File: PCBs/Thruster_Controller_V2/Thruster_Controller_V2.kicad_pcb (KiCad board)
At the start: 4 copper layers, 35.5 x 37 mm, 106 parts, among them J1 PHASE_A, J2 PHASE_B, J3 PHASE_C, J4 Conn_01x01, J5 Pogo Conn, J6 Conn_01x01, J7 Conn_01x01, J8 Conn_01x01, Q1 SIZF906DT, Q2 SIZF906DT, Q3 SIZF906DT, U1 NCP718AMT330, U2 TMS320F280041C, U3 DRV8320S, U8 MCP2562, Y1 20 MHz

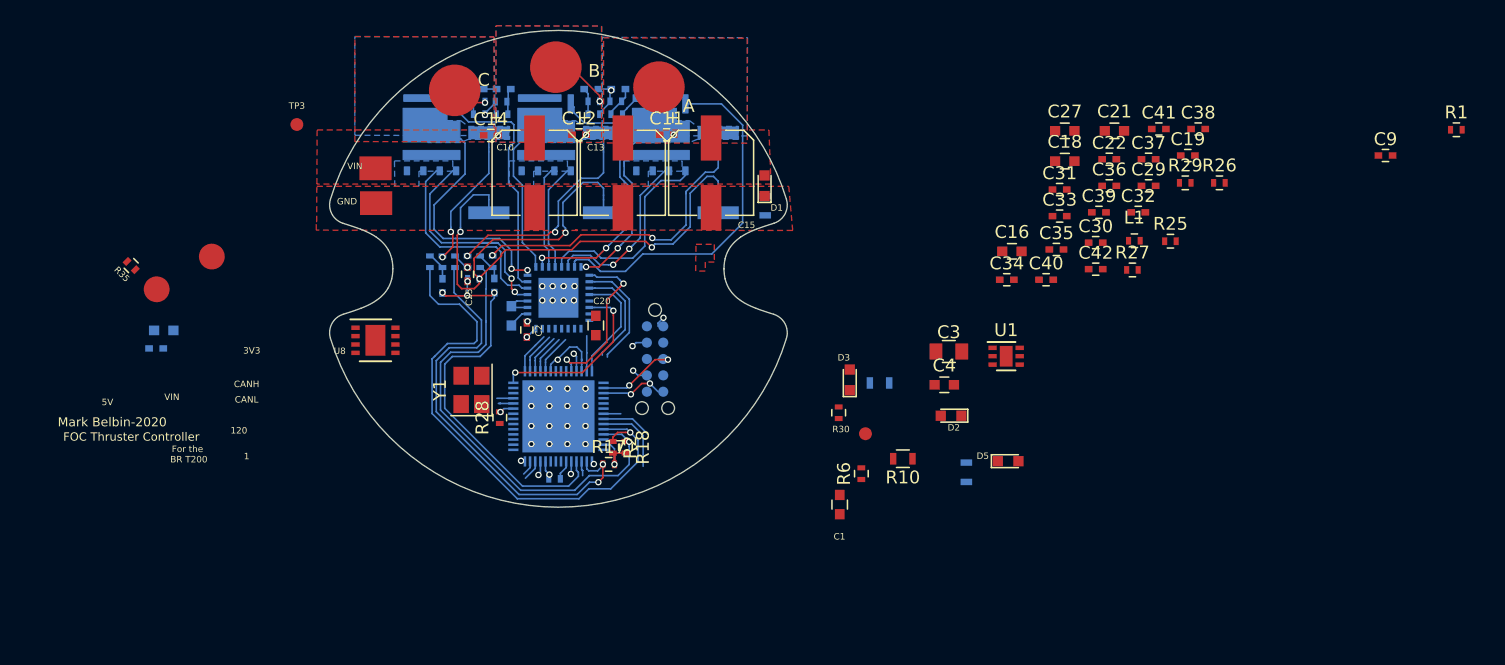
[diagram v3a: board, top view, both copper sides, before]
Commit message: Layout Complete
- Initial layout complete
- Most routing complete, still need to clean up everything.
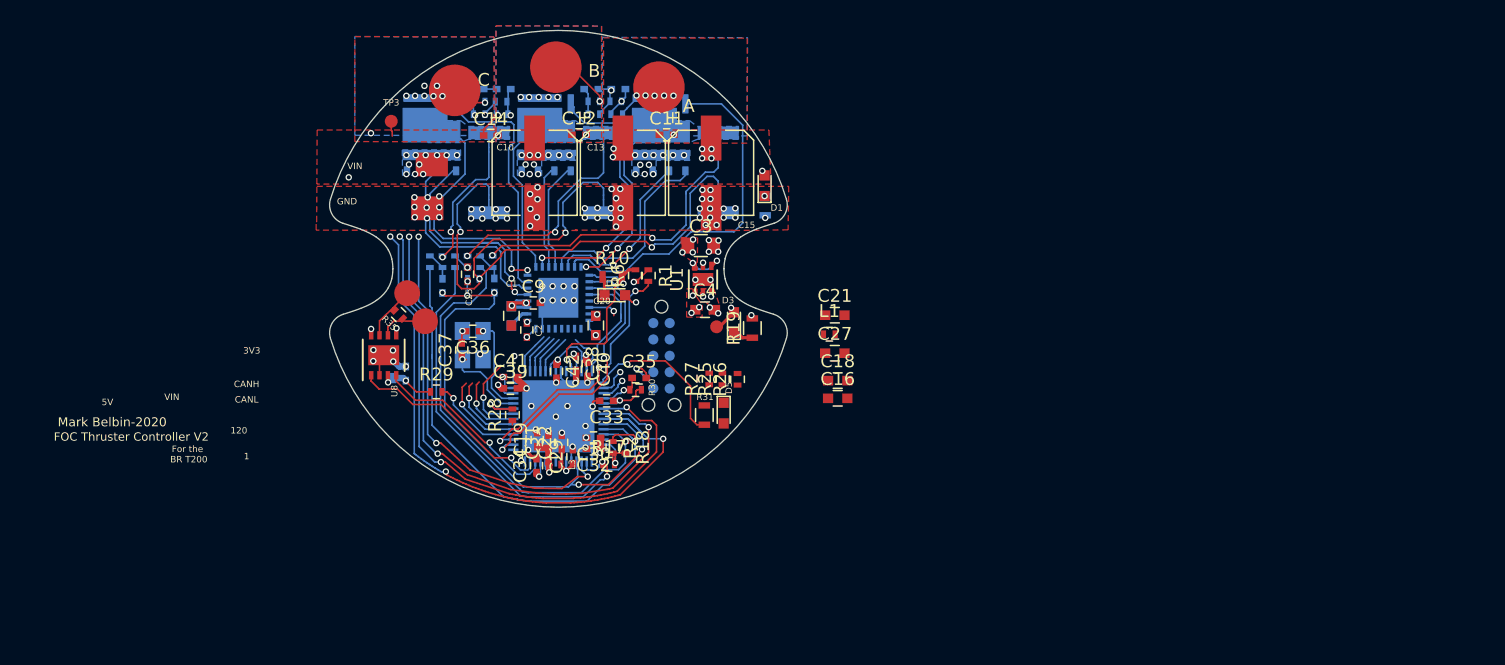
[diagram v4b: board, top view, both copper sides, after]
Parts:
- L3, R19, R31: moved to F.Cu
- Y1: footprint Crystals:Crystal_SMD_SeikoEpson_FA238-4pin_3.2x2.5mm -> Thruster_Controller:Crystal_SMD_SeikoEpson_FA238-4pin_3.2x2.5mm; moved to B.Cu
- moved C9 67.1 mm to (98.0, 100.9)
- moved R1 63.7 mm to (107.0, 98.8), turned to 270 degrees
- moved R29 60.3 mm to (90.5, 107.8)
- moved C37 55.3 mm to (92.5, 104.5), turned to 90 degrees
- moved C19 55.1 mm to (98.3, 111.5), turned to 90 degrees
- moved C41 53.9 mm to (96.3, 106.7)
- moved C38 51.6 mm to (101.4, 105.6), turned to 270 degrees
- moved C36 50.7 mm to (93.3, 103.1), turned to 180 degrees
- moved C29 49.4 mm to (101.1, 112.8), turned to 90 degrees
- moved C22 47.8 mm to (100.2, 111.7), turned to 90 degrees
- moved C39 47.7 mm to (96.3, 107.5)
- moved C32 46.1 mm to (102.7, 112.2), turned to 180 degrees
- moved C31 44.3 mm to (99.2, 111.7), turned to 90 degrees
- moved C42 42.6 mm to (99.8, 106.2), turned to 270 degrees
- moved C30 41.8 mm to (102.7, 111.4), turned to 180 degrees
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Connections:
- C17 pad 1: /Powertrain/VSEN_C -> /Powertrain/VSEN_PVDD
- R15 pad 2: /Powertrain/VSEN_C -> /Powertrain/VSEN_PVDD
- R16 pad 1: /Powertrain/VSEN_C -> /Powertrain/VSEN_PVDD
- U2 pad 6: /Powertrain/VSEN_C -> /Powertrain/VSEN_PVDD
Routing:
- net /Powertrain/VSEN_PVDD: track 0.00 -> 67.2 mm, vias 0 -> 4
- net /Powertrain/VSEN_B: track 3.41 -> 70.6 mm, vias 0 -> 4
- net /Powertrain/VSEN_A: track 6.06 -> 69.1 mm, vias 0 -> 4
- net /Powertrain/VSEN_C: track 5.67 -> 63.5 mm, vias 0 -> 4
- net GND: track 11.7 -> 29.5 mm, vias 30 -> 98
- net +3V3: track 2.94 -> 20.7 mm, vias 2 -> 13
- net /Powertrain/SPI_MOSI: track 8.13 -> 24.9 mm, vias 0 -> 2
- net /Powertrain/SPI_MISO: track 8.86 -> 24.3 mm, vias 0 -> 3
- net /TXCAN: track 1.18 -> 16.3 mm, vias 0 -> 1
- net /RXCAN: track 1.61 -> 15.1 mm, vias 0 -> 1
- net /TI_MCU/GPIO6: track 0.00 -> 12.2 mm, vias 0 -> 1
- net +BATT: track 2.71 -> 12.3 mm, vias 0 -> 50
- net /Powertrain/EN_GATE: track 13.8 -> 4.47 mm
- net /TI_MCU/GPIO24: track 0.00 -> 7.20 mm, vias 0 -> 1
- net /TCK: track 0.00 -> 6.63 mm, vias 0 -> 1
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- added copper zone on In1.Cu, net +3.3VA
- added copper zone on F.Cu, net +3V3
- added copper zone on In1.Cu, net +3V3
- removed copper zone on In2.Cu, net +3V3
- removed copper zone on In2.Cu, net +BATT
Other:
- board text added: "FOC Thruster Controller V2"
- board text removed: "FOC Thruster Controller"

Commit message: Initial Routing and Layout
- Completed all routing, all connections made and zero DRC errors.
- Some courtyard errors but they are irrelevant
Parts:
- C5: moved to F.Cu
- L1: moved to B.Cu
- moved C21 35.3 mm to (87.0, 109.1), turned to 270 degrees
- moved C27 33.6 mm to (88.3, 110.4), turned to 270 degrees
- moved L1 33.5 mm to (88.0, 108.5), turned to 270 degrees
- moved C18 10.5 mm to (111.7, 110.1)
- moved R25 9.00 mm to (108.7, 98.8), turned to 270 degrees
- moved C16 7.73 mm to (114.3, 106.0), turned to 270 degrees
- moved R26 6.10 mm to (109.3, 110.8)
- moved R28 4.36 mm to (92.1, 109.7), turned to 0 degrees
- moved R31 2.25 mm to (111.4, 107.3)
- moved R27 2.15 mm to (111.0, 104.8)
- moved R7 1.94 mm to (115.1, 91.7)
- moved D5 1.88 mm to (112.8, 107.6)
- moved C20 1.72 mm to (101.5, 101.7), turned to 180 degrees
- moved C5 1.40 mm to (95.0, 101.9)
- moved R30 0.46 mm to (106.5, 107.6)
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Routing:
- net /TDO: track 5.95 -> 34.4 mm, vias 1 -> 2
- net /TCK: track 6.63 -> 32.1 mm, vias 1 -> 2
- net /Powertrain/SPI_CS: track 0.32 -> 21.9 mm, vias 1 -> 4
- net /TMS: track 5.34 -> 25.8 mm, vias 1 -> 3
- net /TDI: track 6.39 -> 26.5 mm, vias 1 -> 3
- net +3V3: track 20.7 -> 31.7 mm, vias 13 -> 21
- net /Powertrain/INL_C: track 3.45 -> 13.6 mm, vias 0 -> 2
- net /Powertrain/EN_GATE: track 4.47 -> 14.5 mm
- net /SCI_RX: track 1.92 -> 11.2 mm
- net GND: track 29.5 -> 38.2 mm, vias 98 -> 97
- net /Powertrain/nFAULT: track 14.6 -> 19.0 mm, vias 2 -> 4
- net /SCI_TX: track 2.11 -> 6.41 mm, vias 1 -> 2
- net /Powertrain/SPI_MOSI: track 24.9 -> 22.0 mm
- net Net-(D1-Pad1): track 0.05 -> 2.59 mm
- net /TI_MCU/GPIO6: track 12.2 -> 10.2 mm, vias 1 -> 3
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- added copper zone on In2.Cu, net +BATT

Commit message: Touch-ups
- Routing touchups and plane work
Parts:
- C23, C28: moved to F.Cu
- U8: moved to B.Cu
- moved TP3 3.95 mm to (84.8, 90.0)
- moved J6 1.62 mm to (89.3, 98.9)
- moved J7 1.01 mm to (89.9, 89.2)
- moved J4 0.83 mm to (90.3, 101.8)
- moved C28 0.73 mm to (86.6, 105.4)
- moved C23 0.68 mm to (87.8, 105.8)
- moved U8 0.58 mm to (87.0, 104.8)
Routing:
- net /RXCAN: track 15.1 -> 17.4 mm, vias 1 -> 2
- net /Powertrain/GH_A: track 18.0 -> 16.2 mm
- net /CANH: track 4.39 -> 5.68 mm, vias 0 -> 1
- net +BATT: track 13.4 -> 12.3 mm, vias 50 -> 56
- net /TXCAN: track 16.3 -> 15.3 mm, vias 1 -> 2
- net /Powertrain/SNA: track 54.4 -> 55.1 mm
- net /Powertrain/SL_A: track 22.1 -> 21.5 mm
- net /Powertrain/SH_A: track 16.3 -> 15.7 mm
- net /Powertrain/GL_B: track 22.2 -> 22.8 mm
- net /Powertrain/VSEN_C: track 63.7 -> 64.2 mm
- net GND: track 38.2 -> 38.0 mm, vias 97 -> 109
- net /CANL: track 3.92 -> 3.97 mm, vias 0 -> 1
- net +3V3: vias 21 -> 20
- net /Powertrain/Phase_B: vias 6 -> 36
- net /Powertrain/Phase_C: vias 5 -> 26
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- added copper zone on B.Cu, net GND

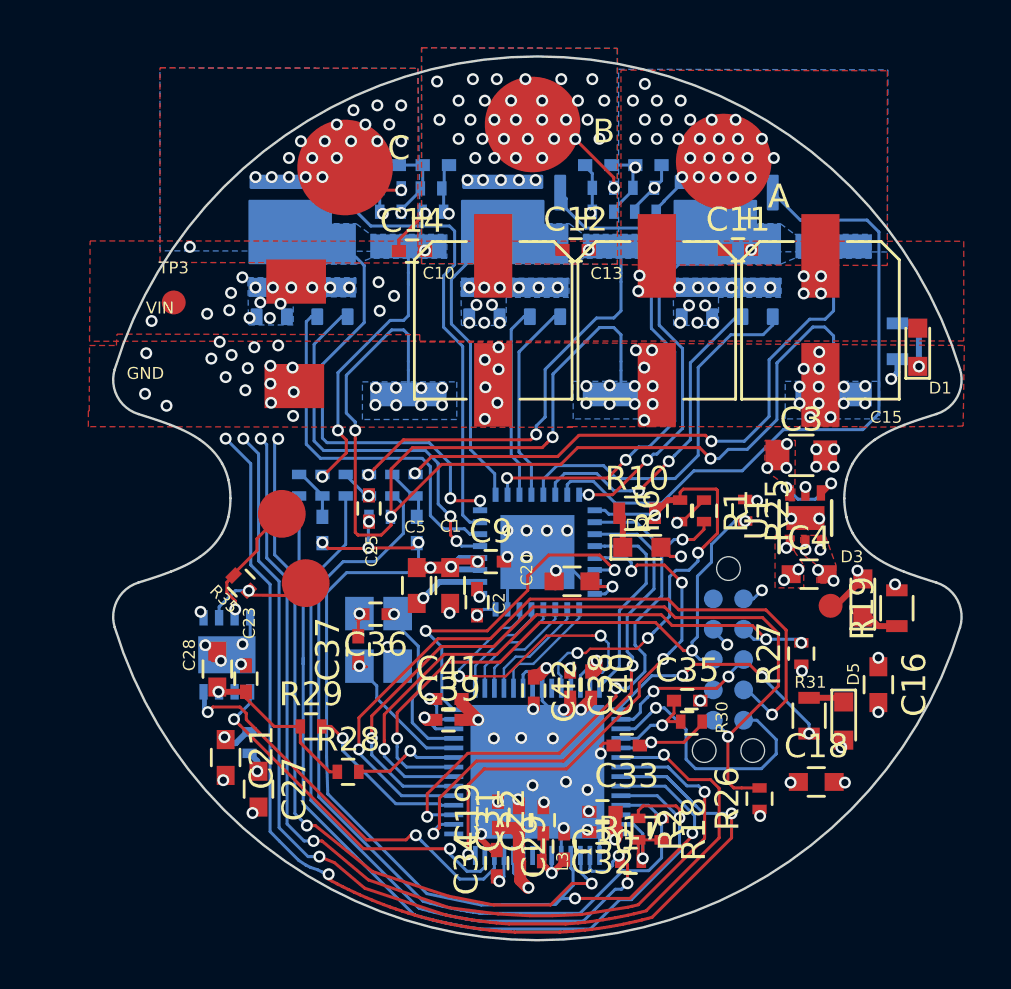
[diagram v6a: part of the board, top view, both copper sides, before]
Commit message: Voltage Feedback Passives
- Changed voltage feedback passives so they aren't right next to the fets this time.
- Should help with soldering, was difficult on V1.
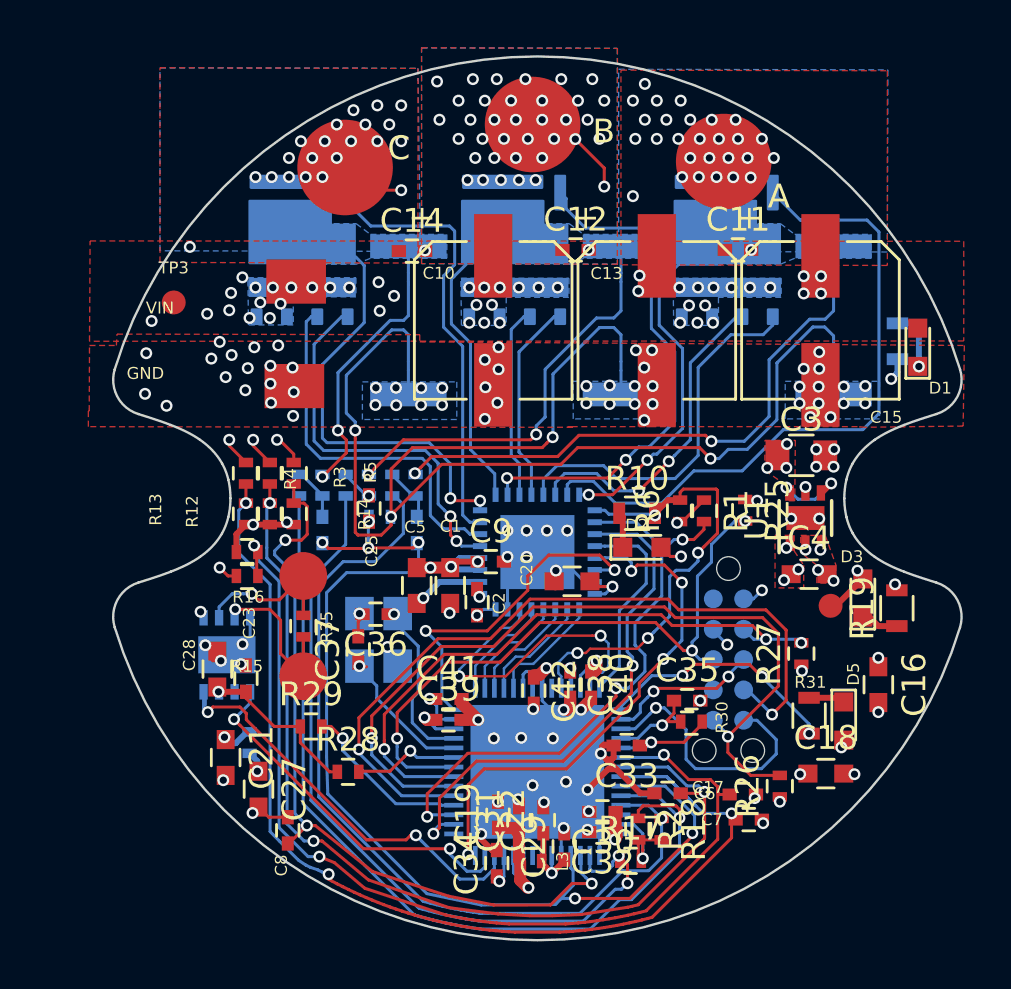
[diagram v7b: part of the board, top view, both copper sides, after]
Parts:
- C17, C6, C7, C8, R12, R13, R14, R15, R16, R3, R4, R5: moved to F.Cu
- moved C8 31.7 mm to (89.5, 112.2), turned to 90 degrees
- moved C7 31.3 mm to (108.8, 111.7)
- moved C17 29.3 mm to (108.6, 110.7), turned to 0 degrees
- moved C6 26.5 mm to (105.5, 110.6), turned to 180 degrees
- moved R14 20.0 mm to (89.8, 98.9), turned to 270 degrees
- moved R12 18.8 mm to (88.8, 98.9), turned to 270 degrees
- moved R3 18.4 mm to (88.8, 97.2), turned to 270 degrees
- moved R5 18.4 mm to (89.8, 97.2), turned to 270 degrees
- moved R15 17.1 mm to (87.8, 101.5)
- moved R16 17.1 mm to (87.8, 100.5)
- moved R13 14.0 mm to (87.8, 98.9), turned to 270 degrees
- moved R4 13.4 mm to (87.8, 97.2), turned to 270 degrees
- moved J6 6.86 mm to (90.2, 105.7)
- moved R35 3.16 mm to (90.2, 103.6), turned to 270 degrees
- moved R26 1.00 mm to (110.2, 110.3)
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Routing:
- net /Powertrain/VSEN_C: track 64.2 -> 32.0 mm, vias 4 -> 3
- net /Powertrain/VSEN_B: track 70.6 -> 41.4 mm, vias 4 -> 3
- net /Powertrain/Phase_B: track 3.88 -> 32.0 mm, vias 36 -> 37
- net /Powertrain/Phase_C: track 3.06 -> 29.2 mm, vias 26 -> 28
- net /Powertrain/VSEN_PVDD: track 67.2 -> 41.7 mm, vias 4 -> 3
- net /Powertrain/VSEN_A: track 69.0 -> 47.2 mm, vias 4 -> 3
- net /Powertrain/Phase_A: track 2.26 -> 22.3 mm, vias 20 -> 21
- net GND: track 38.0 -> 42.5 mm, vias 109 -> 111
- net /CANL: track 3.97 -> 6.58 mm
- net +BATT: track 12.3 -> 11.0 mm
- net /CANH: track 5.68 -> 6.84 mm

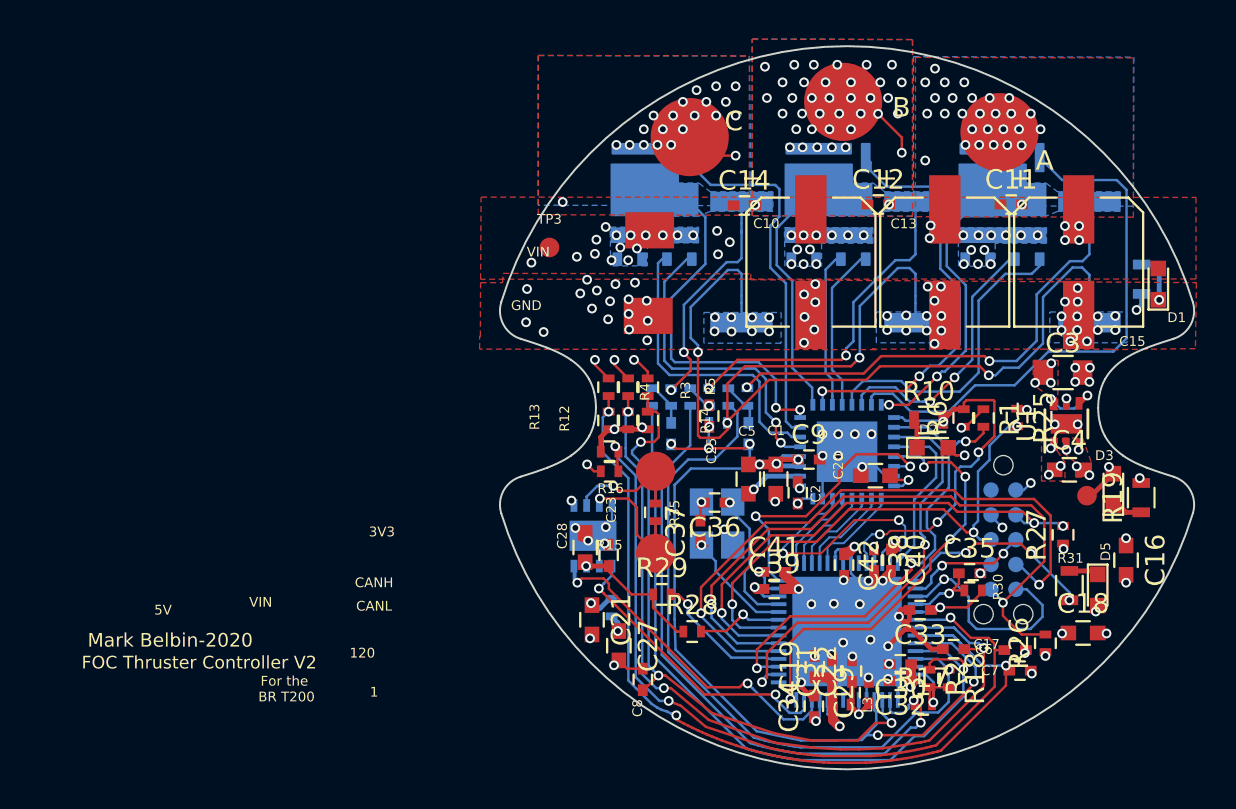
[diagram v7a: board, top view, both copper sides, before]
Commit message: Silkscreen
- Cleaned up all the silkscreen.
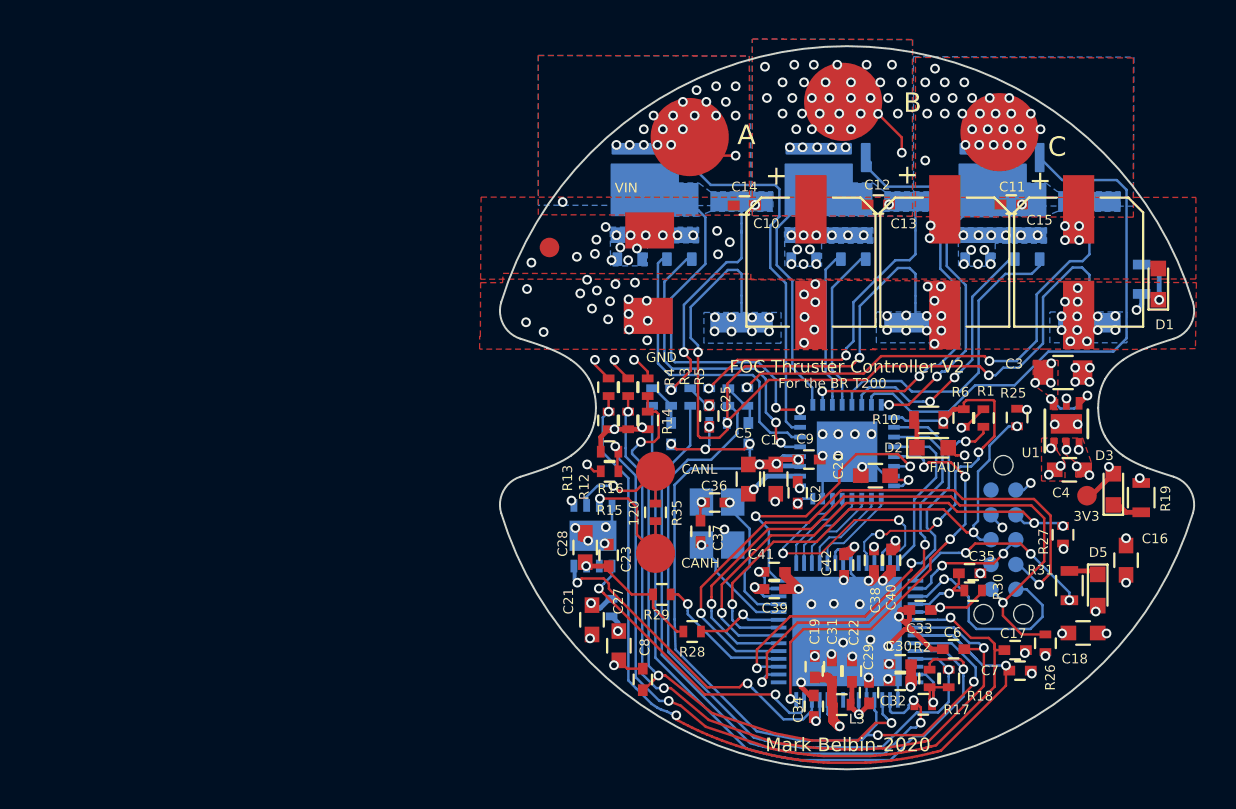
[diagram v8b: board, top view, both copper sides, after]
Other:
- board text added: "FAULT"
- board text removed: "1"
- board text removed: "5V"
